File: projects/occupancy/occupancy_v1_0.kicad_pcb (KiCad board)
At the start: 2 copper layers, 67 x 61 mm, 17 parts, among them J1 Screw_Terminal_01x02, J2 Conn_01x03_Female, J3 Screw_Terminal_01x02, J4 Conn_01x01, K1 JQC-3F-1C-DC5V, Q1 BC547, U1 Easy-Power, U2 LM555

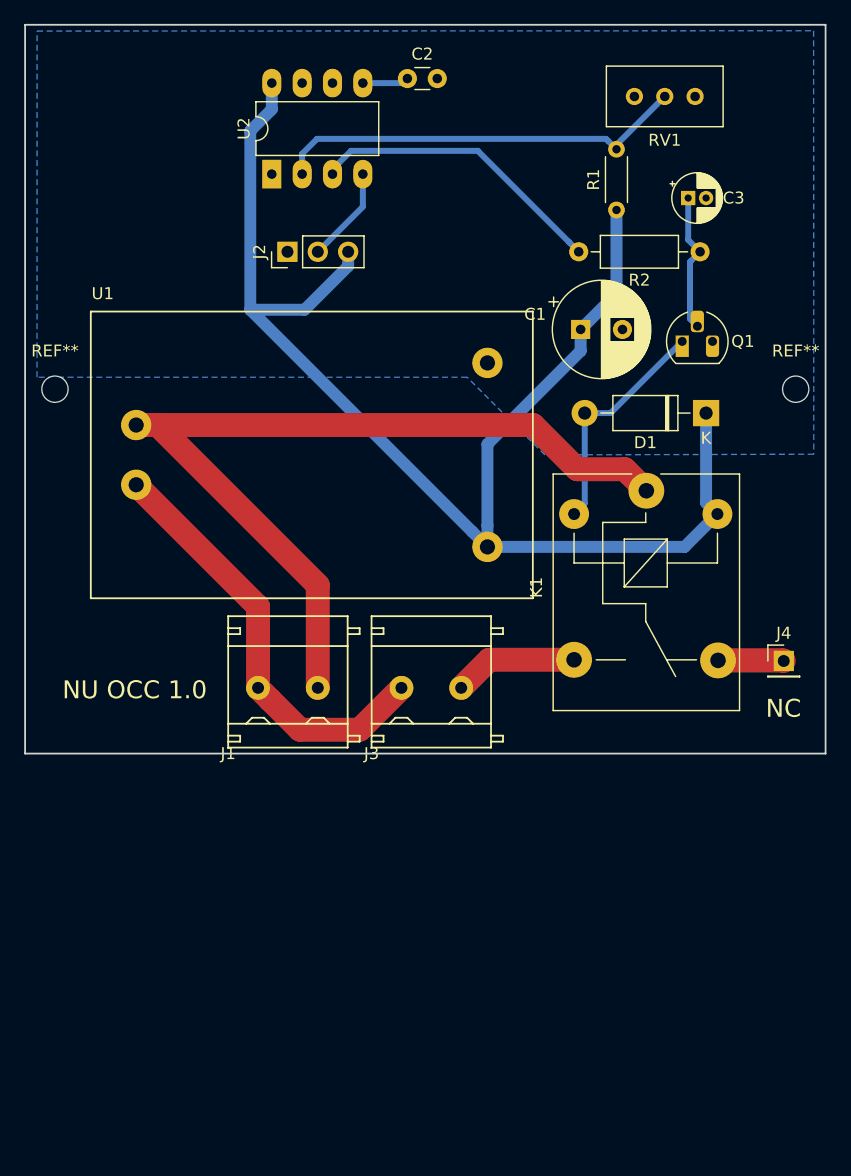
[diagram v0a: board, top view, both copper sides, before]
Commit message: layout wIth the GP box dimensions
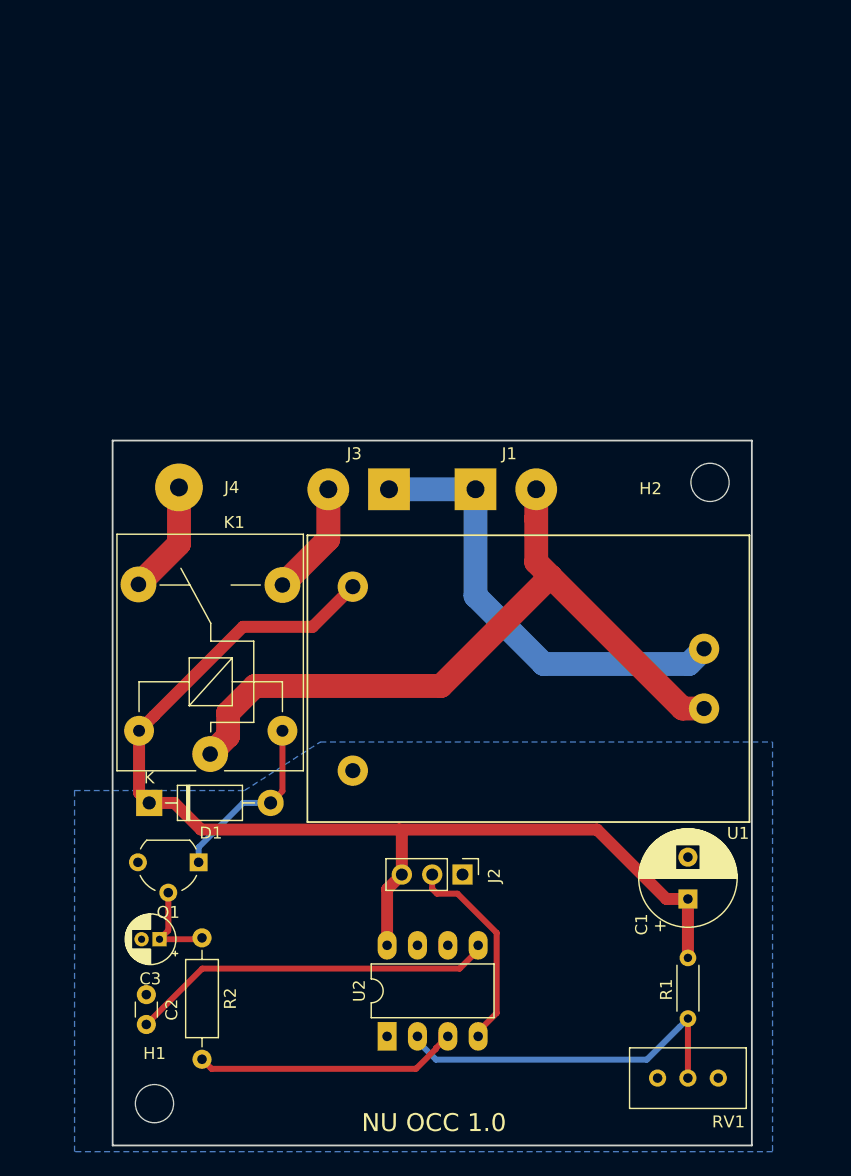
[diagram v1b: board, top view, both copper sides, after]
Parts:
- removed REF** (x2): MountingHole_2.2mm_M2, MountingHole:MountingHole_2.2mm_M2
- added H1: MountingHole, MountingHole:MountingHole_3.2mm_M3, F.Cu at (110.8, 143.3)
- added H2: MountingHole, MountingHole:MountingHole_3.2mm_M3, F.Cu at (157.3, 91.3)
- J1, J3: value Screw_Terminal_01x02 -> Conn_01x02; footprint mylibs:Screw_terminal_2pin_P5mm_width10mm -> Connector_Wire:SolderWirePad_1x02_P5.08mm_Drill1.5mm
- J4: footprint Connector_PinHeader_2.54mm:PinHeader_1x01_P2.54mm_Vertical -> Connector_Wire:SolderWirePad_1x01_Drill1.5mm
- Q1: footprint Package_TO_SOT_THT:TO-92_HandSolder -> Package_TO_SOT_THT:TO-92_Wide
- moved RV1 82.5 mm to (158.0, 141.2), turned to 0 degrees
- moved C2 82.1 mm to (110.2, 136.7), turned to 90 degrees
- moved C3 76.2 mm to (111.3, 129.5), turned to 180 degrees
- moved U2 72.8 mm to (130.3, 137.7)
- moved R2 71.0 mm to (114.8, 129.4), turned to 270 degrees
- moved R1 62.9 mm to (155.5, 131.1), turned to 270 degrees
- moved Q1 59.5 mm to (114.5, 123.1), turned to 180 degrees
- moved D1 56.9 mm to (110.4, 118.1), turned to 0 degrees
- moved U1 55.4 mm to (160.6, 95.7), turned to 180 degrees
- moved J2 54.1 mm to (136.6, 124.1), turned to 270 degrees
- moved J4 52.7 mm to (112.9, 91.7), turned to 90 degrees
- moved C1 48.5 mm to (155.5, 126.2), turned to 90 degrees
- moved K1 42.6 mm to (115.5, 114.0), turned to 90 degrees
- moved J1 29.9 mm to (137.7, 91.9)
- moved J3 21.7 mm to (130.5, 91.9), turned to 180 degrees
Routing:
- net VCC: track 120.6 -> 92.9 mm
- net Net-(C2-Pad1): track 3.89 -> 30.8 mm
- net Net-(J1-Pad2): track 74.3 -> 61.0 mm
- net Net-(J2-Pad2): track 8.06 -> 17.4 mm
- net Net-(R1-Pad2): track 35.0 -> 30.1 mm
- net Net-(D1-Pad2): track 19.5 -> 15.3 mm
- net Net-(J4-Pad1): track 5.63 -> 9.52 mm
- net Net-(C3-Pad1): track 11.8 -> 8.33 mm
- net Net-(R2-Pad2): track 25.2 -> 22.5 mm
- net Net-(J1-Pad1): track 36.1 -> 38.2 mm
- net Net-(J3-Pad2): track 10.4 -> 9.60 mm
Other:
- board size 67 x 61 mm -> 53.5 x 59 mm
- board text added: "OUT"
- board text removed: "NO-OUT"

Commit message: New files modified files etc
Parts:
- added J5: Conn_01x01, Connector_Wire:SolderWirePad_1x01_Drill1.5mm, F.Cu at (143.1, 91.9)
- J1, J3: value Conn_01x02 -> Conn_01x01; footprint Connector_Wire:SolderWirePad_1x02_P5.08mm_Drill1.5mm -> Connector_Wire:SolderWirePad_1x01_Drill1.5mm
- moved J3 5.41 mm to (125.0, 91.9)
- moved J1 3.65 mm to (134.1, 91.9), turned to 180 degrees
- moved H1 1.06 mm to (110.1, 144.1)
- moved H2 1.06 mm to (158.1, 90.5)
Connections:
- J3 pad 1: Net-(J1-Pad1) -> Net-(J3-Pad1)
- K1 pad 1: Net-(J1-Pad2) -> Net-(J1-Pad1)
- K1 pad 3: Net-(J3-Pad2) -> Net-(J3-Pad1)
- U1 pad 1: Net-(J1-Pad2) -> Net-(J1-Pad1)
- U1 pad 2: Net-(J1-Pad1) -> Net-(J5-Pad1)
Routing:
- net Net-(J1-Pad2): track 61.0 -> 0.00 mm
- net Net-(J1-Pad1): track 38.2 -> 64.3 mm
- net Net-(J5-Pad1): track 0.00 -> 19.3 mm
- net Net-(J3-Pad2): track 9.60 -> 0.00 mm
- net Net-(J3-Pad1): track 0.00 -> 9.47 mm

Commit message: Cost XLS and v1.1 and changes
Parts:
- C1: value 470uF -> 470uF,16V
- C3: value 10uF -> 10uF,16V
- U2: value LM555 -> NE555
- moved RV1 0.21 mm to (158.0, 140.9)
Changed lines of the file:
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@@
   (general
     (thickness 1.6)
-    (drawings 32)
-    (tracks 66)
+    (drawings 34)
+    (tracks 67)
     (zones 0)
     (modules 18)
@@
       (effects (font (size 1 1) (thickness 0.15)))
     )
-    (fp_text value 470uF (at -3.81 0 180) (layer F.Fab)
+    (fp_text value 470uF,16V (at -3.81 0 180) (layer F.Fab)
       (effects (font (size 1 1) (thickness 0.15)))
     )
@@
       (effects (font (size 1 1) (thickness 0.15)))
     )
-    (fp_text value 10uF (at 5.08 1.27 180) (layer F.Fab)
+    (fp_text value 10uF,16V (at 5.08 1.27 180) (layer F.Fab)
       (effects (font (size 1 1) (thickness 0.15)))
     )
@@
   )
   (module Potentiometer_THT:Potentiometer_Bourns_3296W_Vertical (layer F.Cu)
-    (at 158.02 141.16)
+    (at 158.015 140.95)
     (descr "Potentiometer, vertical, Bourns 3296W, https://www.bourns.com/pdfs/3296.pdf")
     (tags "Potentiometer vertical Bourns 3296W")
@@
       (effects (font (size 1 1) (thickness 0.15)))
     )
-    (fp_text value LM555 (at 3.81 9.95 90) (layer F.Fab)
+    (fp_text value NE555 (at 3.81 9.95 90) (layer F.Fab)
       (effects (font (size 1 1) (thickness 0.15)))
     )
@@
       (net 12 "Net-(J5-Pad1)"))
   )
-  (dimension 8.900035 (width 0.3) (layer Dwgs.User)
-    (gr_text "8.900 mm" (at 156.320725 177.134406 359.8390572) (layer Dwgs.User)
+  (gr_arc (start 160.825 146.8) (end 160.825 143.8) (angle -90) (layer Dwgs.User) (width 0.15))
+  (gr_arc (start 107.325 87.8) (end 107.325 90.8) (angle -90) (layer Dwgs.User) (width 0.15))
+  (dimension 8.900035 (width 0.3) (layer Cmts.User)
+    (gr_text "8.900 mm" (at 156.320725 177.134406 359.8390572) (layer Cmts.User)
       (effects (font (size 1.5 1.5) (thickness 0.3)))
     )
@@
     (arrow2b (pts (xy 151.876624 175.021914) (xy 153.004771 174.43866)))
   )
-  (dimension 6.800184 (width 0.3) (layer Dwgs.User)
-    (gr_text "6.800 mm" (at 193.969108 143.708964 89.5787151) (layer Dwgs.User)
+  (dimension 6.875 (width 0.3) (layer Cmts.User)
+    (gr_text "6.875 mm" (at 193.95108 143.4375 270) (layer Cmts.User)
       (effects (font (size 1.5 1.5) (thickness 0.3)))
     )
-    (feature1 (pts (xy 151.925 146.8) (xy 192.43057 147.097835)))
-    (feature2 (pts (xy 151.975 140) (xy 192.48057 140.297835)))
-    (crossbar (pts (xy 191.894165 140.293523) (xy 191.844165 147.093523)))
-    (arrow1a (pts (xy 191.844165 147.093523) (xy 191.266043 145.962738)))
-    (arrow1b (pts (xy 191.844165 147.093523) (xy 192.438853 145.971361)))
-    (arrow2a (pts (xy 191.894165 140.293523) (xy 191.299477 141.415685)))
-    (arrow2b (pts (xy 191.894165 140.293523) (xy 192.472287 141.424308)))
-  )
-  (dimension 5.300059 (width 0.3) (layer Dwgs.User)
-    (gr_text "5.300 mm" (at 158.28125 161.462494 0.2702611065) (layer Dwgs.User)
+    (feature1 (pts (xy 151.975 146.875) (xy 192.437501 146.875)))
+    (feature2 (pts (xy 151.975 140) (xy 192.437501 140)))
+    (crossbar (pts (xy 191.85108 140) (xy 191.85108 146.875)))
+    (arrow1a (pts (xy 191.85108 146.875) (xy 191.264659 145.748496)))
+    (arrow1b (pts (xy 191.85108 146.875) (xy 192.437501 145.748496)))
+    (arrow2a (pts (xy 191.85108 140) (xy 191.264659 141.126504)))
+    (arrow2b (pts (xy 191.85108 140) (xy 192.437501 141.126504)))
+  )
+  (dimension 5.300059 (width 0.3) (layer Cmts.User)
+    (gr_text "5.300 mm" (at 158.28125 161.462494 0.2702611065) (layer Cmts.User)
       (effects (font (size 1.5 1.5) (thickness 0.3)))
     )
@@
   )
   (gr_line (start 151.05 138.85) (end 152.9 141.15) (layer Dwgs.User) (width 0.15))
-  (dimension 26.700105 (width 0.3) (layer Dwgs.User)
-    (gr_text "26.700 mm" (at 147.474788 155.587017 0.1609427776) (layer Dwgs.User)
+  (dimension 26.700105 (width 0.3) (layer Cmts.User)
+    (gr_text "26.700 mm" (at 147.474788 155.587017 0.1609427776) (layer Cmts.User)
       (effects (font (size 1.5 1.5) (thickness 0.3)))
     )
@@
     (arrow2b (pts (xy 134.118889 153.524525) (xy 135.243741 152.934942)))
   )
-  (dimension 26.775 (width 0.3) (layer Dwgs.User)
-    (gr_text "26.775 mm" (at 120.6875 155.55) (layer Dwgs.User)
+  (dimension 26.700012 (width 0.3) (layer Cmts.User)
+    (gr_text "26.700 mm" (at 120.641784 155.587496 -0.05364771795) (layer Cmts.User)
       (effects (font (size 1.5 1.5) (thickness 0.3)))
     )
-    (feature1 (pts (xy 107.3 146.8) (xy 107.3 154.036421)))
-    (feature2 (pts (xy 134.075 146.8) (xy 134.075 154.036421)))
-    (crossbar (pts (xy 134.075 153.45) (xy 107.3 153.45)))
-    (arrow1a (pts (xy 107.3 153.45) (xy 108.426504 152.863579)))
-    (arrow1b (pts (xy 107.3 153.45) (xy 108.426504 154.036421)))
-    (arrow2a (pts (xy 134.075 153.45) (xy 132.948496 152.863579)))
-    (arrow2b (pts (xy 134.075 153.45) (xy 132.948496 154.036421)))
-  )
-  (dimension 13.175024 (width 0.3) (layer Dwgs.User)
-    (gr_text "13.175 mm" (at 177.237494 140.294379 89.89127949) (layer Dwgs.User)
+    (feature1 (pts (xy 107.3 146.8) (xy 107.293201 154.061418)))
+    (feature2 (pts (xy 134 146.825) (xy 133.993201 154.086418)))
+    (crossbar (pts (xy 133.99375 153.499997) (xy 107.29375 153.474997)))
+    (arrow1a (pts (xy 107.29375 153.474997) (xy 108.420802 152.889631)))
+    (arrow1b (pts (xy 107.29375 153.474997) (xy 108.419704 154.062472)))
+    (arrow2a (pts (xy 133.99375 153.499997) (xy 132.867796 152.912522)))
+    (arrow2b (pts (xy 133.99375 153.499997) (xy 132.866698 154.085363)))
+  )
+  (dimension 13.200095 (width 0.3) (layer Cmts.User)
+    (gr_text "13.200 mm" (at 177.224762 140.388446 89.78297157) (layer Cmts.User)
       (effects (font (size 1.5 1.5) (thickness 0.3)))
     )
-    (feature1 (pts (xy 134.1 133.625) (xy 175.736418 133.704006)))
-    (feature2 (pts (xy 134.075 146.8) (xy 175.711418 146.879006)))
-    (crossbar (pts (xy 175.124998 146.877894) (xy 175.149998 133.702894)))
-    (arrow1a (pts (xy 175.149998 133.702894) (xy 175.73428 134.830508)))
-    (arrow1b (pts (xy 175.149998 133.702894) (xy 174.561441 134.828283)))
-    (arrow2a (pts (xy 175.124998 146.877894) (xy 175.713555 145.752505)))
-    (arrow2b (pts (xy 175.124998 146.877894) (xy 174.540716 145.75028)))
+    (feature1 (pts (xy 134.1 133.625) (xy 175.736193 133.782713)))
+    (feature2 (pts (xy 134.05 146.825) (xy 175.686193 146.982713)))
+    (crossbar (pts (xy 175.099777 146.980492) (xy 175.149777 133.780492)))
+    (arrow1a (pts (xy 175.149777 133.780492) (xy 175.731927 134.909209)))
+    (arrow1b (pts (xy 175.149777 133.780492) (xy 174.559093 134.904766)))
+    (arrow2a (pts (xy 175.099777 146.980492) (xy 175.690461 145.856218)))
+    (arrow2b (pts (xy 175.099777 146.980492) (xy 174.517627 145.851775)))
   )
   (gr_line (start 122.6 122.1) (end 145.6 122.1) (layer Dwgs.User) (width 0.15))
@@
     (effects (font (size 1.5 1.5) (thickness 0.3)))
   )
-  (gr_line (start 107.325 87.8) (end 160.83 87.8) (layer Edge.Cuts) (width 0.15))
-  (gr_line (start 107.33 146.8) (end 107.325 87.8) (layer Edge.Cuts) (width 0.15))
-  (gr_line (start 160.83 146.8) (end 107.33 146.8) (layer Edge.Cuts) (width 0.15))
-  (gr_line (start 160.83 87.8) (end 160.83 146.8) (layer Edge.Cuts) (width 0.15))
+  (gr_line (start 107.325 87.8) (end 160.825 87.8) (layer Edge.Cuts) (width 0.15))
+  (gr_line (start 107.325 146.8) (end 107.325 87.8) (layer Edge.Cuts) (width 0.15))
+  (gr_line (start 160.825 146.8) (end 107.325 146.8) (layer Edge.Cuts) (width 0.15))
+  (gr_line (start 160.825 87.8) (end 160.825 146.8) (layer Edge.Cuts) (width 0.15))
   (segment (start 110.789999 110.840001) (end 109.54 112.09) (width 1) (layer F.Cu) (net 1))
   (segment (start 124.069999 103.390001) (end 118.239999 103.390001) (width 1) (layer F.Cu) (net 1))
@@
   (segment (start 137.922 137.268) (end 139.47201 135.71799) (width 0.5) (layer F.Cu) (net 7))
   (segment (start 137.922 137.668) (end 137.922 137.268) (width 0.5) (layer F.Cu) (net 7))
-  (segment (start 155.48 136.18) (end 155.48 141.16) (width 0.5) (layer F.Cu) (net 8))
   (segment (start 154.780001 136.879999) (end 155.48 136.18) (width 0.5) (layer B.Cu) (net 8))
   (segment (start 152.04199 139.61801) (end 154.780001 136.879999) (width 0.5) (layer B.Cu) (net 8))
@@
   (segment (start 132.842 138.068) (end 134.39201 139.61801) (width 0.5) (layer B.Cu) (net 8))
   (segment (start 132.842 137.668) (end 132.842 138.068) (width 0.5) (layer B.Cu) (net 8))
+  (segment (start 155.475 136.185) (end 155.48 136.18) (width 0.5) (layer F.Cu) (net 8))
+  (segment (start 155.475 140.95) (end 155.475 136.185) (width 0.5) (layer F.Cu) (net 8))
   (segment (start 135.382 137.668) (end 135.382 138.068) (width 0.5) (layer F.Cu) (net 9))
   (segment (start 115.607999 140.385999) (end 114.808 139.586) (width 0.5) (layer F.Cu) (net 9))
